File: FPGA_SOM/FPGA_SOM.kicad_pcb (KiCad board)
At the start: 6 copper layers, 49 x 47.1 mm, 58 parts, among them J1 Conn_01x12, J2 Conn_02x05_Counter_Clockwise, J3 Conn_01x06, J5 Conn_01x02, J7 Conn_01x09, J8 Conn_01x10, U1 ICE40UP5K-SG48ITR, U2 AP2127N-3.3, U3 AP2127N-1.2, U4 W25X20CLSN, X1 ECS-2520MV-xxx-xx

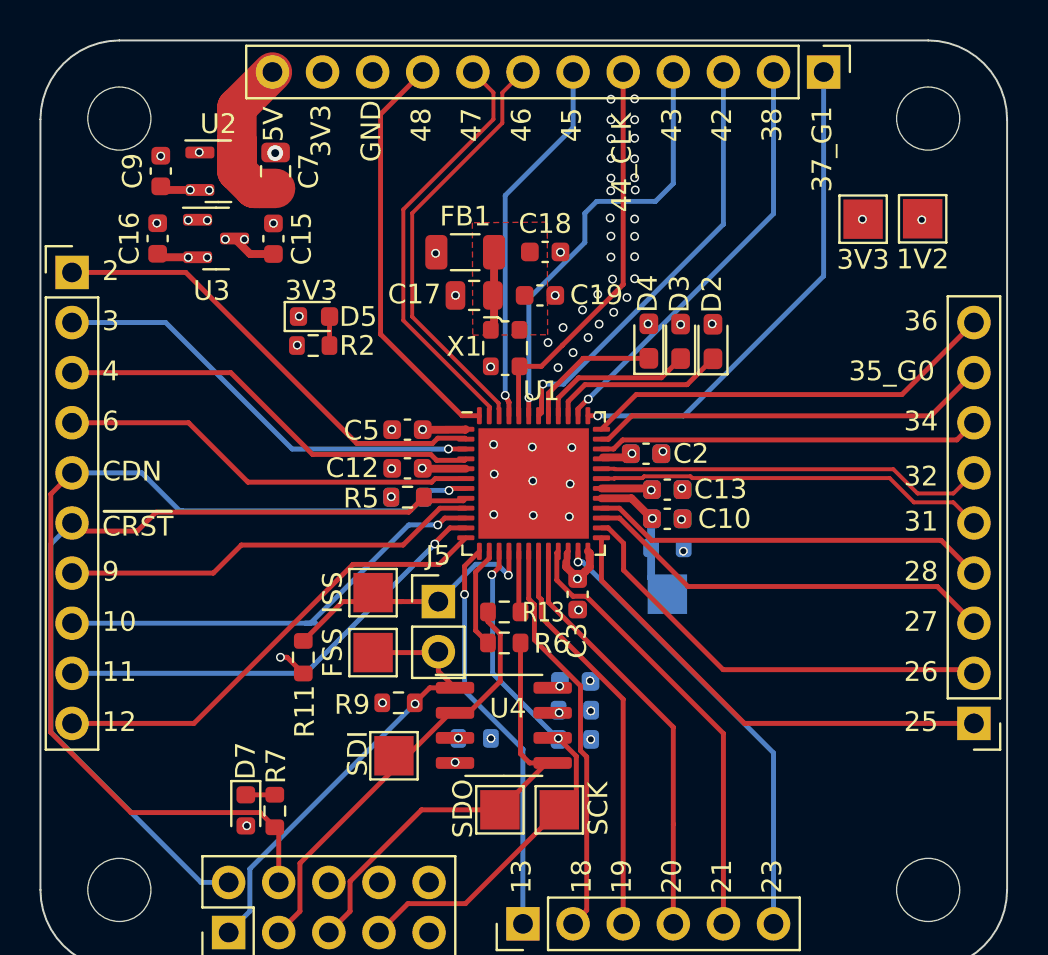
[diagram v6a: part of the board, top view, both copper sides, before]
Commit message: Added button and clarified silkscreen for RGB leds.
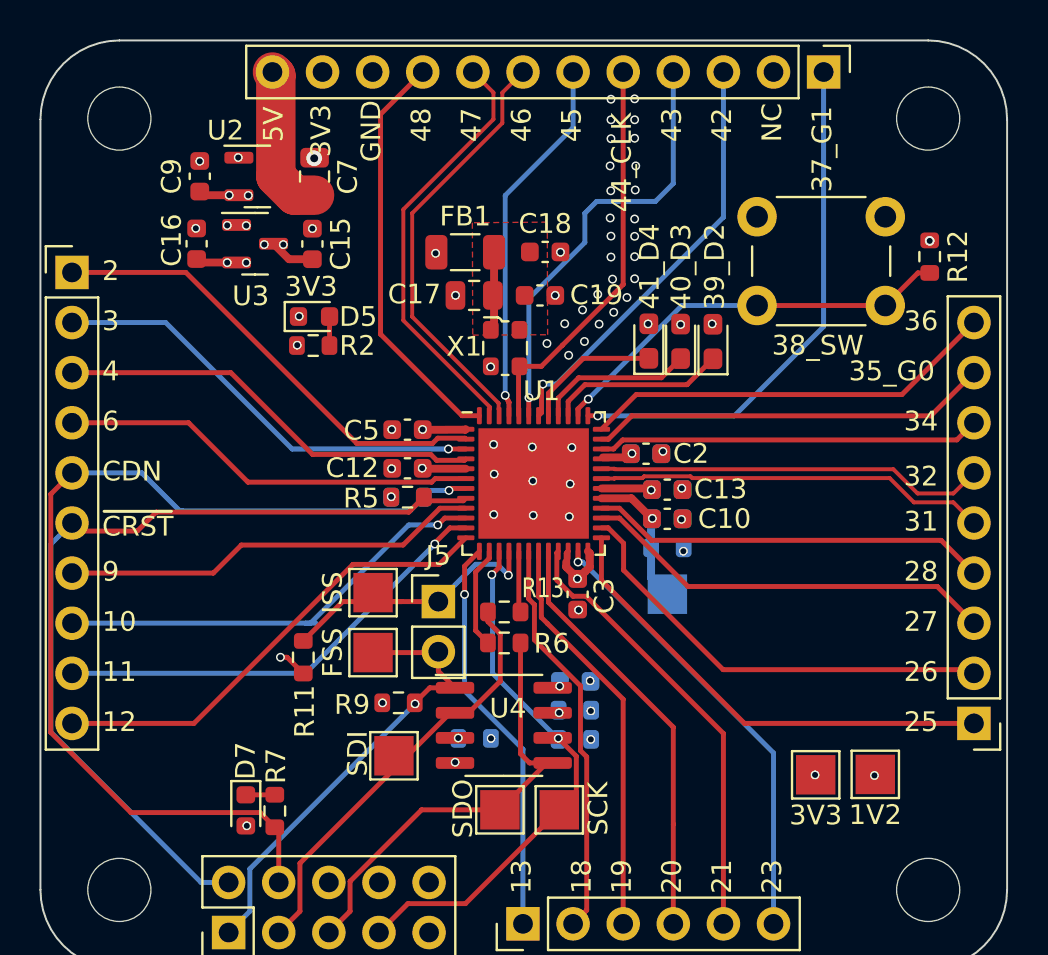
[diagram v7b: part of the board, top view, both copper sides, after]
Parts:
- added 38_SW: SW_Push, Button_Switch_THT:SW_PUSH_6mm, F.Cu at (136.3, 111.5)
- added R12: 10k, Resistor_SMD:R_0603_1608Metric, F.Cu at (145.1, 113.5)
- moved TP4 28.3 mm to (142.3, 139.7)
- moved TP3 28.3 mm to (139.3, 139.8)
- moved C16 1.99 mm to (107.9, 112.8)
- moved C7 1.99 mm to (113.9, 109.4)
- moved C9 1.99 mm to (108.1, 109.4)
- moved U2 1.99 mm to (111.0, 109.4)
- moved U3 1.99 mm to (110.9, 112.8)
- moved C15 1.99 mm to (113.8, 112.9)
- renumbered D2 to 39_D2, D3 to 40_D3, D4 to 41_D4
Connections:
- U1 pad 38: /38 -> /38_button
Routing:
- net /38: track 21.6 -> 0.00 mm, vias 1 -> 0
- net /38_button: track 0.00 -> 21.1 mm, vias 0 -> 1
- net +5V: track 9.38 -> 7.72 mm
- net /37_G1: track 25.2 -> 26.7 mm
- net GND: vias 54 -> 57
- net (no net): vias 5 -> 0
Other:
- board text added: "NC"
- board text removed: "38"

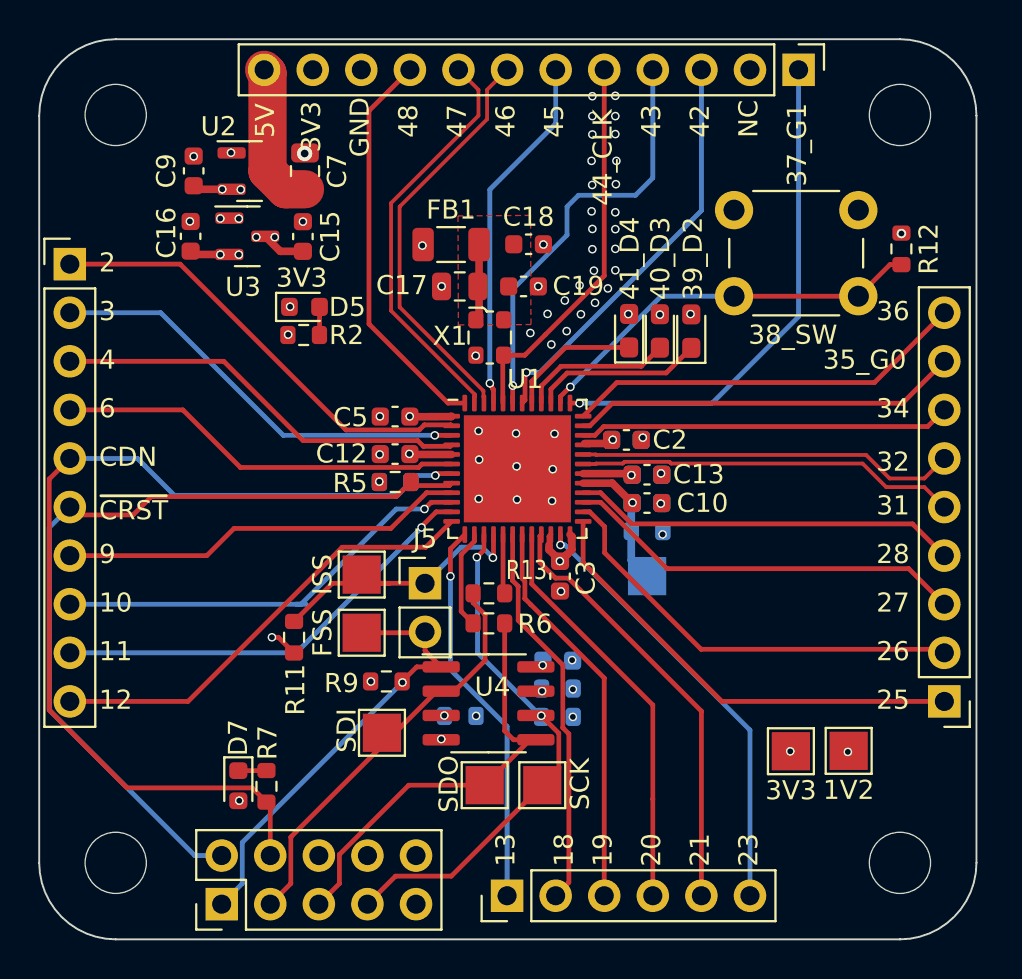
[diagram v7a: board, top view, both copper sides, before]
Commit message: Added silkscreen, stitching vias, and quality of life improvements.
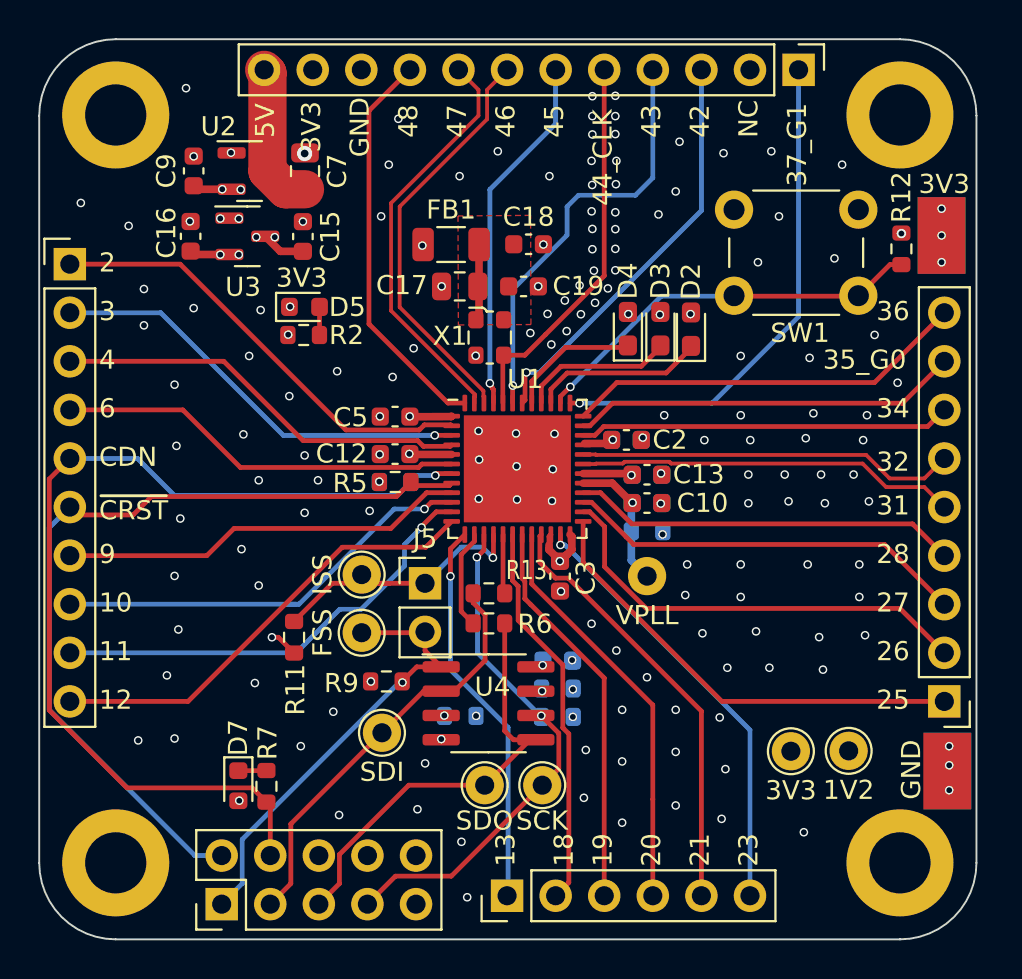
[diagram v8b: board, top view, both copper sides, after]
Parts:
- removed 38_SW: SW_Push, Button_Switch_THT:SW_PUSH_6mm
- removed 39_D2, 40_D3, 41_D4: LED_Small, Diode_SMD:D_0603_1608Metric_Pad1.05x0.95mm_HandSolder
- added ?: , , F.Cu at (147.2, 112.8)
- added ?: , , B.Cu at (147.5, 140.8)
- added ?: , , B.Cu at (147.2, 112.8)
- added D2: LED_Small, Diode_SMD:D_0603_1608Metric_Pad1.05x0.95mm_HandSolder, F.Cu at (134.1, 117.7)
- added D3: LED_Small, Diode_SMD:D_0603_1608Metric_Pad1.05x0.95mm_HandSolder, F.Cu at (132.5, 117.7)
- added D4: LED_Small, Diode_SMD:D_0603_1608Metric_Pad1.05x0.95mm_HandSolder, F.Cu at (130.8, 117.7)
- added REF**: TestPoint_Pad_2.5x2.5mm, TestPoint:TestPoint_Pad_2.5x2.5mm, F.Cu at (147.5, 140.8)
- added SW1: SW_Push, Button_Switch_THT:SW_PUSH_6mm, F.Cu at (136.3, 111.5)
- H1, H2, H3, H4: footprint MountingHole:MountingHole_3.2mm_M3 -> MountingHole:MountingHole_3.2mm_M3_DIN965_Pad
- TP1, TP3, TP4, TP5, TP6, TP7, TP8, TP9: footprint TestPoint:TestPoint_Pad_2.0x2.0mm -> TestPoint:TestPoint_THTPad_D2.0mm_Drill1.0mm
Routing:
- net /11: track 23.0 -> 23.7 mm
- net /3V3: vias 21 -> 23
- net GND: vias 57 -> 160
- net /1V2: vias 6 -> 5
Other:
- board text added: "https://github.com/ Tobi-McKellar/ iCE40UP5k_Breakout"
